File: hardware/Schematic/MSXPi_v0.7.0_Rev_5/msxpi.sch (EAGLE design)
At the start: 36 parts, among them IC1 LD117AS33TR

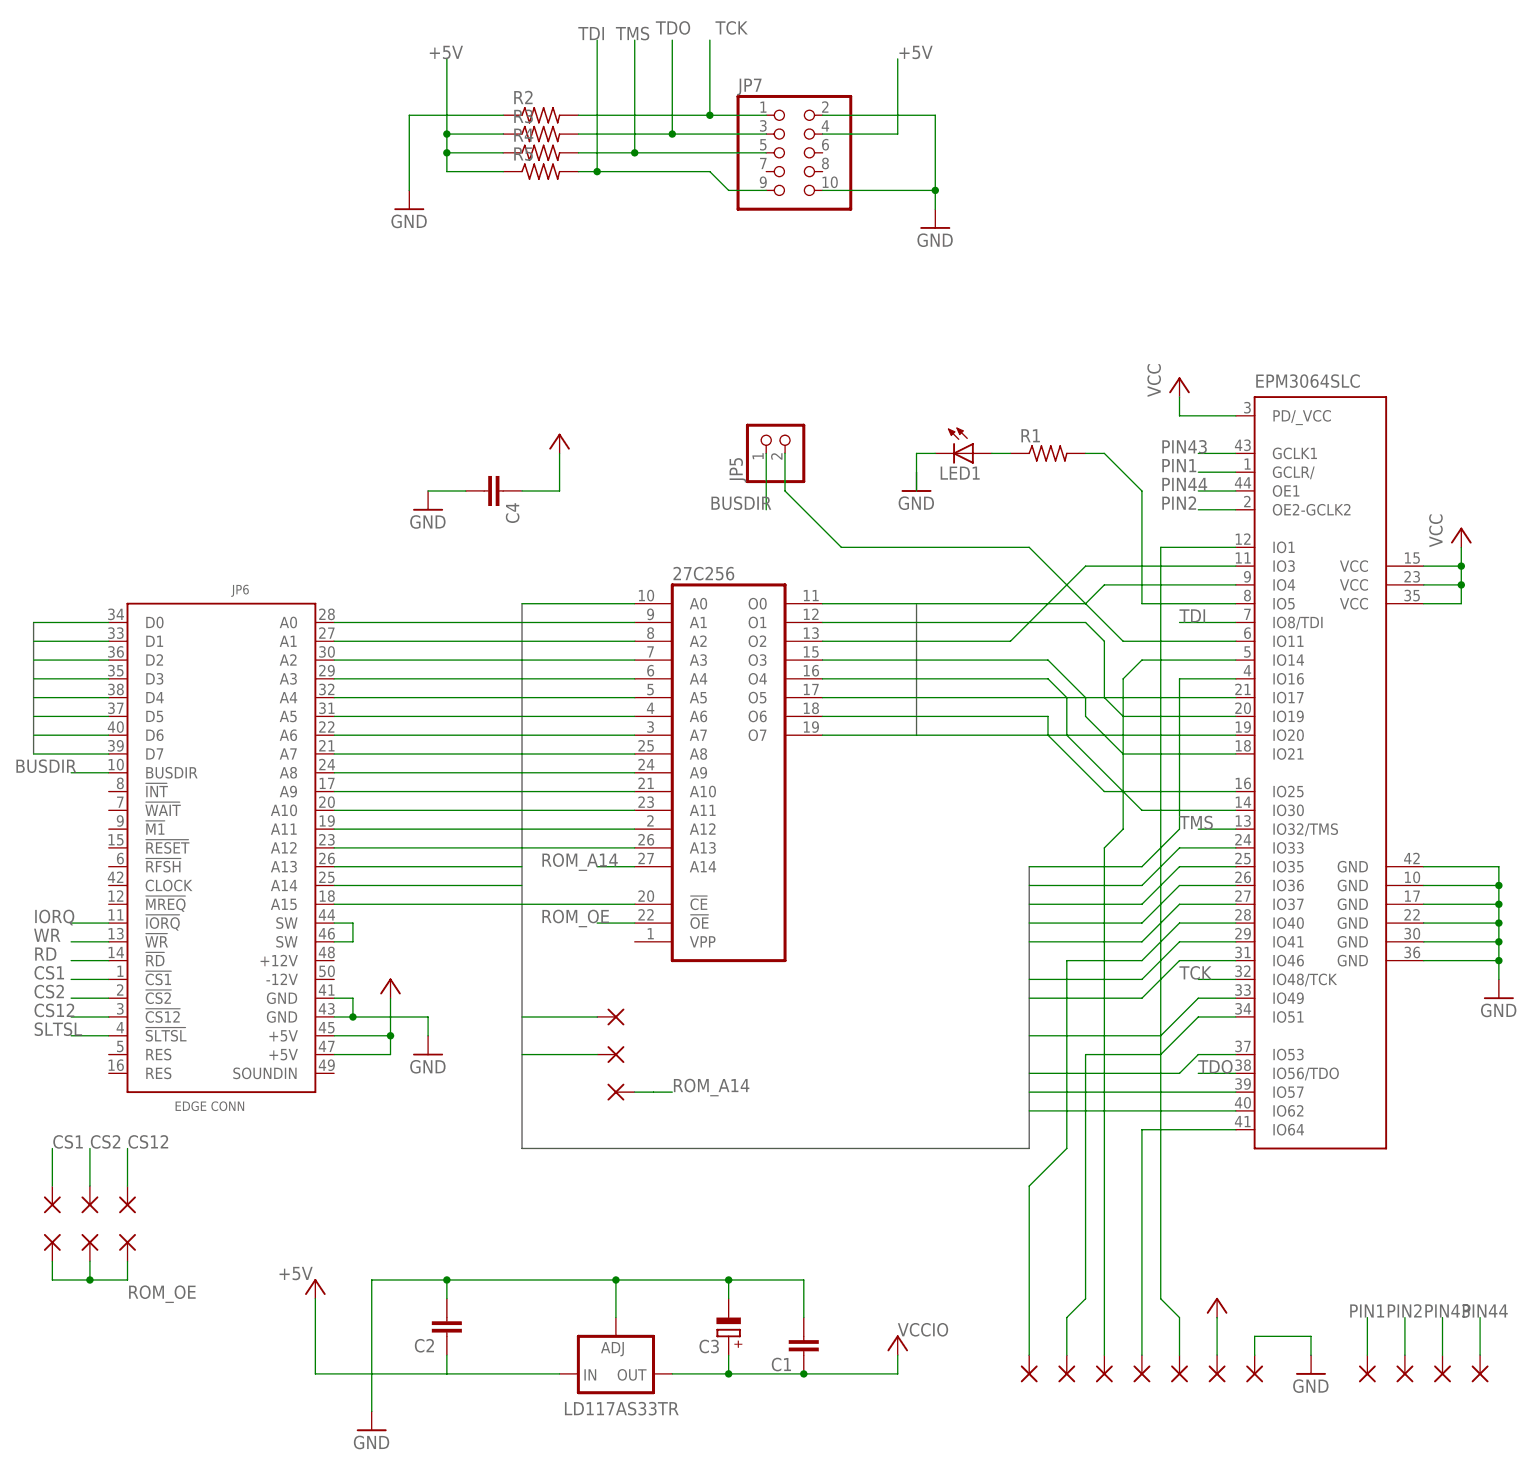
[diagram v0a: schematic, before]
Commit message: Schema update: added jumper to disable Rapsberry Pi VCC
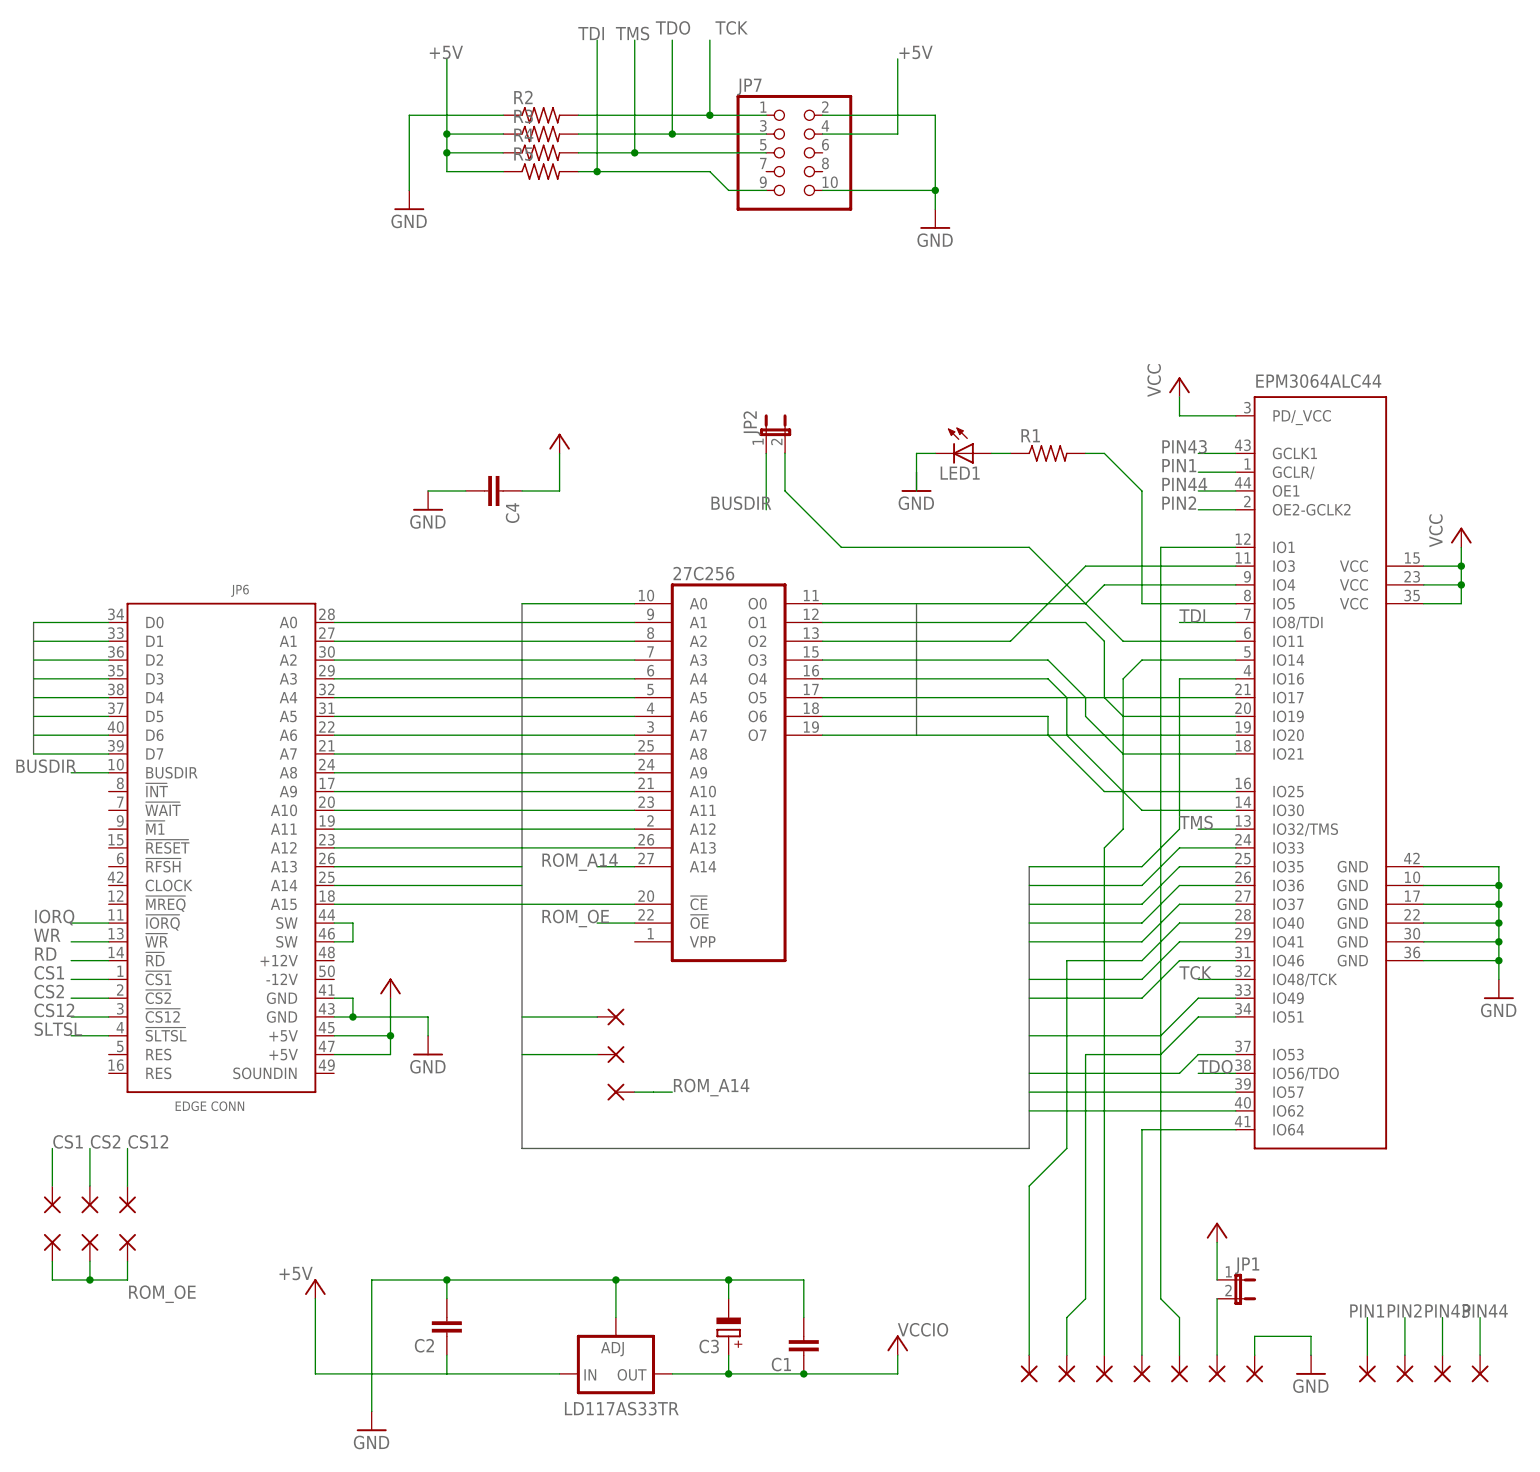
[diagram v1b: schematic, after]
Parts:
- removed JP5: (no value), pinhead:PINHD-1X2
- added JP1, JP2: (no value), jumper:JP1E
- renumbered EPM3064SLC to EPM3064ALC44
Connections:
- new net N$3: +5V.P, JP1.2
- net +5V: now also JP1.1; no longer +5V.P
- net BUSDIR: now also JP2.1; no longer JP5.1
- net MSXR1: now also JP2.2; no longer JP5.2
